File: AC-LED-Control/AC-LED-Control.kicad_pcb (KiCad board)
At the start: 4 copper layers, 120 parts, among them P101 CONN_01X02, P102 CONN_01X02, P103 CONN_01X04, P201 CONN_01X02, P202 CONN_01X02, P203 CONN_01X02, P204 CONN_01X02, P205 CONN_01X02, P206 CONN_01X02, P207 CONN_01X02, P208 CONN_01X02, P301 CONN_01X02, P302 CONN_01X02, P303 CONN_01X02, P304 CONN_01X02, P305 CONN_01X02, P306 CONN_01X02, P307 CONN_01X02, P308 CONN_01X02, SW101 SW_PUSH, U101 FOD814-D, U102 STM32F030F4P6, U103 74HC595, U104 74HC595, U201 LTV-846S, U206 LTV-846S, U301 LTV-846S, U306 LTV-846S

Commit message: Associated LEDs
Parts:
- added D101: LED, LEDs:LED_0805, F.Cu at (6.64, 6.60)
- added D102: LED, LEDs:LED_0805, F.Cu at (12.5, 13.2)
- added D103: LED, LEDs:LED_0805, F.Cu at (-1.52, 6.60)
- added D104: LED, LEDs:LED_0805, F.Cu at (-6.42, 6.60)
- added D105: LED, LEDs:LED_0805, F.Cu at (8.28, 6.60)
- added D106: LED, LEDs:LED_0805, F.Cu at (3.38, 6.60)
- added D107: LED, LEDs:LED_0805, F.Cu at (13.2, 6.60)
- added D108: LED, LEDs:LED_0805, F.Cu at (10.9, 13.2)
- added D109: LED, LEDs:LED_0805, F.Cu at (9.91, 6.60)
- added D110: LED, LEDs:LED_0805, F.Cu at (-4.79, 6.60)
- added D111: LED, LEDs:LED_0805, F.Cu at (1.74, 6.60)
- added D112: LED, LEDs:LED_0805, F.Cu at (0.11, 6.60)
- added D113: LED, LEDs:LED_0805, F.Cu at (-3.16, 6.60)
- added D114: LED, LEDs:LED_0805, F.Cu at (5.01, 6.60)
- added D115: LED, LEDs:LED_0805, F.Cu at (9.25, 13.2)
- added D116: LED, LEDs:LED_0805, F.Cu at (11.5, 6.60)
- added R107: 160, Resistors_SMD:R_0603_HandSoldering, F.Cu at (4.35, 13.2)
- added R108: 160, Resistors_SMD:R_0603_HandSoldering, F.Cu at (7.62, 13.2)
- added R109: 160, Resistors_SMD:R_0603_HandSoldering, F.Cu at (1.09, 13.2)
- added R110: 160, Resistors_SMD:R_0603_HandSoldering, F.Cu at (2.72, 13.2)
- added R111: 160, Resistors_SMD:R_0603_HandSoldering, F.Cu at (-0.54, 13.2)
- added R112: 160, Resistors_SMD:R_0603_HandSoldering, F.Cu at (-3.81, 13.2)
- added R113: 160, Resistors_SMD:R_0603_HandSoldering, F.Cu at (5.99, 13.2)
- added R114: 160, Resistors_SMD:R_0603_HandSoldering, F.Cu at (-2.18, 13.2)
- added U105: VXO7803-1000, power_reg:VXO7803-1000, F.Cu at (22.4, 6.60)
- moved C101 78.3 mm to (112.9, -42.5)
- moved C102 78.3 mm to (112.9, -38.5)
- moved C103 78.3 mm to (111.4, -42.5)
- moved C104 78.3 mm to (114.4, -38.5)
- moved C105 78.3 mm to (114.4, -42.5)
- moved C201 78.3 mm to (48.9, -36.9)
- moved C202 78.3 mm to (0.51, -29.7)
- moved C203 78.3 mm to (29.0, -19.1)
- moved C204 78.3 mm to (44.4, -31.0)
- moved C205 78.3 mm to (2.51, -41.0)
- moved C207 78.3 mm to (-15.2, -41.0)
- moved C208 78.3 mm to (-10.8, -41.0)
- moved C301 78.3 mm to (200.3, -9.75)
- moved C304 78.3 mm to (191.5, -9.75)
- moved C306 78.3 mm to (187.1, -9.75)
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
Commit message: Changed TRIAC from DPAK part to T0-202-3 part.
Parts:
- removed P101, P102, P201, P202, P203, P204, P205, P206, P207, P208, P301, P302, P303, P304, P305, P306, P307, P308: CONN_01X02, Pin_Headers:Pin_Header_Straight_1x02
- removed R217, R218, R219, R220, R317, R318, R319, R320: 660, Resistors_SMD:R_0603_HandSoldering
- removed R221, R222, R223, R224, R225, R226, R227, R228, R229, R230, R231, R232, R321, R322, R323, R324, R325, R326, R327, R328, R329, R330, R331, R332: 56, Resistors_SMD:R_0603_HandSoldering
- removed REF**: Pin_Header_Straight_1x03, Pin_Headers:Pin_Header_Straight_1x03
- added J101: Conn_01x03, Pin_Headers:Pin_Header_Straight_1x03_Pitch2.54mm, F.Cu at (152.8, 151.6)
- added J102: Conn_01x03, Pin_Headers:Pin_Header_Straight_1x03_Pitch2.54mm, F.Cu at (166.6, 148.2)
- added J103: Conn_01x02, Pin_Headers:Pin_Header_Straight_1x02_Pitch2.54mm, F.Cu at (189.2, 137.6)
- added J201: Conn_01x02, Connectors_OnShore:OSTTC022162, F.Cu at (194.2, 119.7)
- added J202: Conn_01x02, Connectors_OnShore:OSTTC022162, F.Cu at (183.5, 119.7)
- added J203: Conn_01x02, Connectors_OnShore:OSTTC022162, F.Cu at (209.0, 93.9)
- added J204: Conn_01x02, Connectors_OnShore:OSTTC022162, F.Cu at (198.3, 106.8)
- added J205: Conn_01x02, Connectors_OnShore:OSTTC022162, F.Cu at (187.5, 106.8)
- added J206: Conn_01x02, Connectors_OnShore:OSTTC022162, F.Cu at (198.3, 93.9)
- added J207: Conn_01x02, Connectors_OnShore:OSTTC022162, F.Cu at (172.7, 115.9)
- added J208: Conn_01x02, Connectors_OnShore:OSTTC022162, F.Cu at (187.5, 93.9)
- added J301: Conn_01x02, Connectors_OnShore:OSTTC022162, F.Cu at (263.4, 119.7)
- added J302: Conn_01x02, Connectors_OnShore:OSTTC022162, F.Cu at (267.4, 93.9)
- added J303: Conn_01x02, Connectors_OnShore:OSTTC022162, F.Cu at (252.6, 115.9)
- added J304: Conn_01x02, Connectors_OnShore:OSTTC022162, F.Cu at (278.2, 93.9)
- added J305: Conn_01x02, Connectors_OnShore:OSTTC022162, F.Cu at (267.4, 106.8)
- added J306: Conn_01x02, Connectors_OnShore:OSTTC022162, F.Cu at (278.2, 106.8)
- added J307: Conn_01x02, Connectors_OnShore:OSTTC022162, F.Cu at (288.9, 93.9)
- added J308: Conn_01x02, Connectors_OnShore:OSTTC022162, F.Cu at (274.1, 119.7)
- added P104: CONN_01X02, Pin_Headers:Pin_Header_Straight_1x02_Pitch2.54mm, F.Cu at (162.6, 160.0)
- added P105: CONN_01X02, Pin_Headers:Pin_Header_Straight_1x02_Pitch2.54mm, F.Cu at (176.4, 148.3)
- added R115: 680, Resistors_SMD:R_0603_HandSoldering, F.Cu at (183.6, 152.5)
- added R116: 680, Resistors_SMD:R_0603_HandSoldering, F.Cu at (196.7, 151.8)
- added U106: IE1203S, SIP-Packages:SIP-4, F.Cu at (143.2, 167.1)
- added U202: TRIAC, Power-Packages:TO-202-3-Vertical, F.Cu at (138.0, 95.2)
- added U203: TRIAC, Power-Packages:TO-202-3-Vertical, F.Cu at (166.0, 95.0)
- added U204: TRIAC, Power-Packages:TO-202-3-Vertical, F.Cu at (125.9, 92.4)
- added U205: TRIAC, Power-Packages:TO-202-3-Vertical, F.Cu at (95.4, 86.4)
- added U207: TRIAC, Power-Packages:TO-202-3-Vertical, F.Cu at (101.7, 86.4)
- added U208: TRIAC, Power-Packages:TO-202-3-Vertical, F.Cu at (108.1, 86.4)
- added U302: TRIAC, Power-Packages:TO-202-3-Vertical, F.Cu at (273.7, 44.2)
- added U303: TRIAC, Power-Packages:TO-202-3-Vertical, F.Cu at (241.9, 45.0)
- added U304: TRIAC, Power-Packages:TO-202-3-Vertical, F.Cu at (235.6, 45.0)
- added U305: TRIAC, Power-Packages:TO-202-3-Vertical, F.Cu at (197.8, 34.8)
- added U307: TRIAC, Power-Packages:TO-202-3-Vertical, F.Cu at (222.9, 45.0)
- added U308: TRIAC, Power-Packages:TO-202-3-Vertical, F.Cu at (267.3, 45.0)
- C201, C202, C203, C204, C205, C206, C207, C208, C301, C302, C303, C304, C305, C306, C307, C308: value 22nF -> 22n
- D101, D102, D103, D104, D105, D106, D107, D108, D109, D110, D111, D112, D113, D114, D115, D116: footprint LEDs:LED_0805 -> LEDs:LED_0603_HandSoldering
- P103: footprint Pin_Headers:Pin_Header_Straight_1x04 -> Pin_Headers:Pin_Header_Straight_1x04_Pitch2.54mm
- R103: value 10K -> 16K
- R201, R202, R301, R302: value 660 -> 56
- R203, R204, R303, R304: value 660 -> 100
- R207, R208, R211, R212, R215, R216, R307, R308, R311, R312, R315, R316: value 56 -> 100
- SW101: footprint Buttons_Switches_SMD:SW_SPST_EVPBF -> Buttons_Switches_THT:SW_PUSH_6mm_h5mm
- U105: value VXO7803-1000 -> LTV-827; footprint power_reg:VXO7803-1000 -> Housings_DIP:DIP-8_W7.62mm
- U201, U206, U301, U306: value LTV-846S -> TRIAC; footprint lite-on:Lite-On_SMD-16 -> Power-Packages:TO-202-3-Vertical
- moved C207 270.1 mm to (210.1, 107.9)
- moved C208 269.1 mm to (210.0, 112.7)
- moved C205 252.8 mm to (210.1, 103.1)
- moved C202 252.4 mm to (201.7, 122.6)
- moved D113 242.6 mm to (188.0, 156.0)
- moved C206 240.3 mm to (205.8, 108.2)
- moved R112 238.4 mm to (178.5, 166.8)
- moved D114 237.7 mm to (200.5, 141.7)
- moved R111 237.5 mm to (192.4, 151.8)
- moved R109 236.9 mm to (196.7, 146.8)
- moved R110 234.0 mm to (182.9, 162.6)
- moved R113 233.9 mm to (187.2, 161.1)
- moved D110 233.5 mm to (174.1, 156.7)
- moved R114 230.7 mm to (178.5, 156.7)
- moved R215 230.1 mm to (174.9, 125.3)
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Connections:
- D102 pad 2: Net-(D102-Pad2) -> /CHAN8
- D104 pad 2: Net-(D104-Pad2) -> /CHAN9
- D106 pad 2: Net-(D106-Pad2) -> /CHAN10
- D108 pad 2: Net-(D108-Pad2) -> /CHAN11
- D109 pad 2: /Output-BankB/OUT-A -> Net-(D109-Pad2)
- D110 pad 2: /Output-BankB/OUT-B -> /CHAN12
- D111 pad 2: /Output-BankB/OUT-C -> Net-(D111-Pad2)
- D112 pad 2: /Output-BankB/OUT-D -> /CHAN13
- D113 pad 2: /Output-BankB/OUT-E -> Net-(D113-Pad2)
- D114 pad 2: /Output-BankB/OUT-F -> /CHAN14
- D115 pad 2: /Output-BankB/OUT-G -> Net-(D115-Pad2)
- D116 pad 2: /Output-BankB/OUT-H -> /CHAN15
- R104 pad 1: +3V3 -> /3v3_ISO
- R105 pad 1: +3V3 -> /3v3_ISO
- R107 pad 2: /Output-BankA/OUT-A -> /CHAN0
- R108 pad 1: Net-(D102-Pad2) -> Net-(D103-Pad2)
- R108 pad 2: /Output-BankA/OUT-B -> /CHAN1
- R109 pad 1: Net-(D103-Pad2) -> Net-(D105-Pad2)
- R109 pad 2: /Output-BankA/OUT-C -> /CHAN2
- R110 pad 1: Net-(D104-Pad2) -> Net-(D107-Pad2)
- R110 pad 2: /Output-BankA/OUT-D -> /CHAN3
- R111 pad 1: Net-(D105-Pad2) -> Net-(D109-Pad2)
- R111 pad 2: /Output-BankA/OUT-E -> /CHAN4
- R112 pad 1: Net-(D106-Pad2) -> Net-(D111-Pad2)
- R112 pad 2: /Output-BankA/OUT-F -> /CHAN5
- R113 pad 1: Net-(D107-Pad2) -> Net-(D113-Pad2)
- R113 pad 2: /Output-BankA/OUT-G -> /CHAN6
- R114 pad 1: Net-(D108-Pad2) -> Net-(D115-Pad2)
- R114 pad 2: /Output-BankA/OUT-H -> /CHAN7
- R201 pad 1: Net-(R201-Pad1) -> /Output-BankA/AC_LOAD-A
- R201 pad 2: /Output-BankA/OUT-A -> Net-(C201-Pad2)
- R202 pad 1: Net-(R202-Pad1) -> /Output-BankA/AC_LOAD-E
- R202 pad 2: /Output-BankA/OUT-B -> Net-(C202-Pad2)
- R203 pad 2: /Output-BankA/OUT-C -> /CHAN0
- R204 pad 2: /Output-BankA/OUT-D -> /CHAN4
- R205 pad 1: Net-(R205-Pad1) -> /Output-BankA/AC_LOAD-B
- R205 pad 2: AC-N -> Net-(C203-Pad2)
- R206 pad 1: Net-(R206-Pad1) -> /Output-BankA/AC_LOAD-F
- R206 pad 2: AC-N -> Net-(C204-Pad2)
- R207 pad 2: AC-N -> /CHAN1
- R208 pad 2: AC-N -> /CHAN5
- R209 pad 1: Net-(C201-Pad2) -> /Output-BankA/AC_LOAD-C
- R209 pad 2: Net-(R209-Pad2) -> Net-(C205-Pad2)
- R210 pad 1: Net-(C202-Pad2) -> /Output-BankA/AC_LOAD-G
- R210 pad 2: Net-(R210-Pad2) -> Net-(C206-Pad2)
- R211 pad 1: Net-(C203-Pad2) -> Net-(R211-Pad1)
- R211 pad 2: Net-(R211-Pad2) -> /CHAN2
- R212 pad 1: Net-(C204-Pad2) -> Net-(R212-Pad1)
- R212 pad 2: Net-(R212-Pad2) -> /CHAN6
- R213 pad 1: /Output-BankA/AC_LOAD-A -> /Output-BankA/AC_LOAD-D
- R213 pad 2: Net-(C201-Pad2) -> Net-(C207-Pad2)
- R214 pad 1: /Output-BankA/AC_LOAD-B -> /Output-BankA/AC_LOAD-H
- R214 pad 2: Net-(C202-Pad2) -> Net-(C208-Pad2)
- R215 pad 1: /Output-BankA/AC_LOAD-C -> Net-(R215-Pad1)
- R215 pad 2: Net-(C203-Pad2) -> /CHAN3
- R216 pad 1: /Output-BankA/AC_LOAD-D -> Net-(R216-Pad1)
- R216 pad 2: Net-(C204-Pad2) -> /CHAN7
- R301 pad 1: Net-(R301-Pad1) -> /Output-BankB/AC_LOAD-A
- R301 pad 2: /Output-BankB/OUT-A -> Net-(C301-Pad2)
- R302 pad 1: Net-(R302-Pad1) -> /Output-BankB/AC_LOAD-E
- R302 pad 2: /Output-BankB/OUT-B -> Net-(C302-Pad2)
- R303 pad 2: /Output-BankB/OUT-C -> /CHAN8
- R304 pad 2: /Output-BankB/OUT-D -> /CHAN12
- R305 pad 1: Net-(R305-Pad1) -> /Output-BankB/AC_LOAD-B
- R305 pad 2: AC-N -> Net-(C303-Pad2)
- R306 pad 1: Net-(R306-Pad1) -> /Output-BankB/AC_LOAD-F
- R306 pad 2: AC-N -> Net-(C304-Pad2)
- R307 pad 2: AC-N -> /CHAN9
- R308 pad 2: AC-N -> /CHAN13
- R309 pad 1: Net-(C301-Pad2) -> /Output-BankB/AC_LOAD-C
- R309 pad 2: Net-(R309-Pad2) -> Net-(C305-Pad2)
- R310 pad 1: Net-(C302-Pad2) -> /Output-BankB/AC_LOAD-G
- R310 pad 2: Net-(R310-Pad2) -> Net-(C306-Pad2)
- R311 pad 1: Net-(C303-Pad2) -> Net-(R311-Pad1)
- R311 pad 2: Net-(R311-Pad2) -> /CHAN10
- R312 pad 1: Net-(C304-Pad2) -> Net-(R312-Pad1)
- R312 pad 2: Net-(R312-Pad2) -> /CHAN14
- R313 pad 1: /Output-BankB/AC_LOAD-A -> /Output-BankB/AC_LOAD-D
- R313 pad 2: Net-(C301-Pad2) -> Net-(C307-Pad2)
- R314 pad 1: /Output-BankB/AC_LOAD-B -> /Output-BankB/AC_LOAD-H
- R314 pad 2: Net-(C302-Pad2) -> Net-(C308-Pad2)
- R315 pad 1: /Output-BankB/AC_LOAD-C -> Net-(R315-Pad1)
- R315 pad 2: Net-(C303-Pad2) -> /CHAN11
- R316 pad 1: /Output-BankB/AC_LOAD-D -> Net-(R316-Pad1)
- R316 pad 2: Net-(C304-Pad2) -> /CHAN15
- U102 pad 17: /I2C_SCL -> /STM_SCL
- U102 pad 18: /I2C_SDA -> /STM_SDA
- U103 pad 1: /Output-BankA/OUT-B -> /CHAN1
- U103 pad 15: /Output-BankA/OUT-A -> /CHAN0
- U103 pad 2: /Output-BankA/OUT-C -> /CHAN2
- U103 pad 3: /Output-BankA/OUT-D -> /CHAN3
- U103 pad 4: /Output-BankA/OUT-E -> /CHAN4
- U103 pad 5: /Output-BankA/OUT-F -> /CHAN5
- U103 pad 6: /Output-BankA/OUT-G -> /CHAN6
- U103 pad 7: /Output-BankA/OUT-H -> /CHAN7
- U104 pad 1: /Output-BankB/OUT-B -> /CHAN9
- U104 pad 15: /Output-BankB/OUT-A -> /CHAN8
- U104 pad 2: /Output-BankB/OUT-C -> /CHAN10
- U104 pad 3: /Output-BankB/OUT-D -> /CHAN11
- U104 pad 4: /Output-BankB/OUT-E -> /CHAN12
- U104 pad 5: /Output-BankB/OUT-F -> /CHAN13
- U104 pad 6: /Output-BankB/OUT-G -> /CHAN14
- U104 pad 7: /Output-BankB/OUT-H -> /CHAN15
- U105 pad 1: /+12V_IN -> /STM_SCL
- U105 pad 3: +3V3 -> /STM_SDA
- U201 pad 1: Net-(R201-Pad1) -> AC-N
- U201 pad 2: GND -> /Output-BankA/AC_LOAD-A
- U201 pad 3: Net-(R202-Pad1) -> Net-(R203-Pad1)
- U206 pad 1: Net-(R217-Pad1) -> AC-N
- U206 pad 2: GND -> /Output-BankA/AC_LOAD-G
- U206 pad 3: Net-(R218-Pad1) -> Net-(R212-Pad1)
- U301 pad 1: Net-(R301-Pad1) -> AC-N
- U301 pad 2: GND -> /Output-BankB/AC_LOAD-A
- U301 pad 3: Net-(R302-Pad1) -> Net-(R303-Pad1)
- U306 pad 1: Net-(R317-Pad1) -> AC-N
- U306 pad 2: GND -> /Output-BankB/AC_LOAD-G
- U306 pad 3: Net-(R318-Pad1) -> Net-(R312-Pad1)
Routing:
- net +3V3: track 26.1 -> 0.00 mm
- net /STM_~RST: track 17.3 -> 0.00 mm
- net /STM_SWDIO: track 10.7 -> 0.00 mm
- net /I2C_SDA: track 9.93 -> 0.00 mm
- net /I2C_SCL: track 9.82 -> 0.00 mm
- net /STM_SWCLK: track 8.39 -> 0.00 mm
- net GND: track 5.75 -> 0.00 mm
- net /ZERO_CROSS: track 2.58 -> 0.00 mm
- net Net-(R102-Pad1): track 2.27 -> 0.00 mm
- net Net-(R101-Pad1): track 2.27 -> 0.00 mm
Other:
- board text removed: "OUTA"
- board text removed: "OUTD"
- board text removed: "OUTE"
- board text removed: "OUTH"

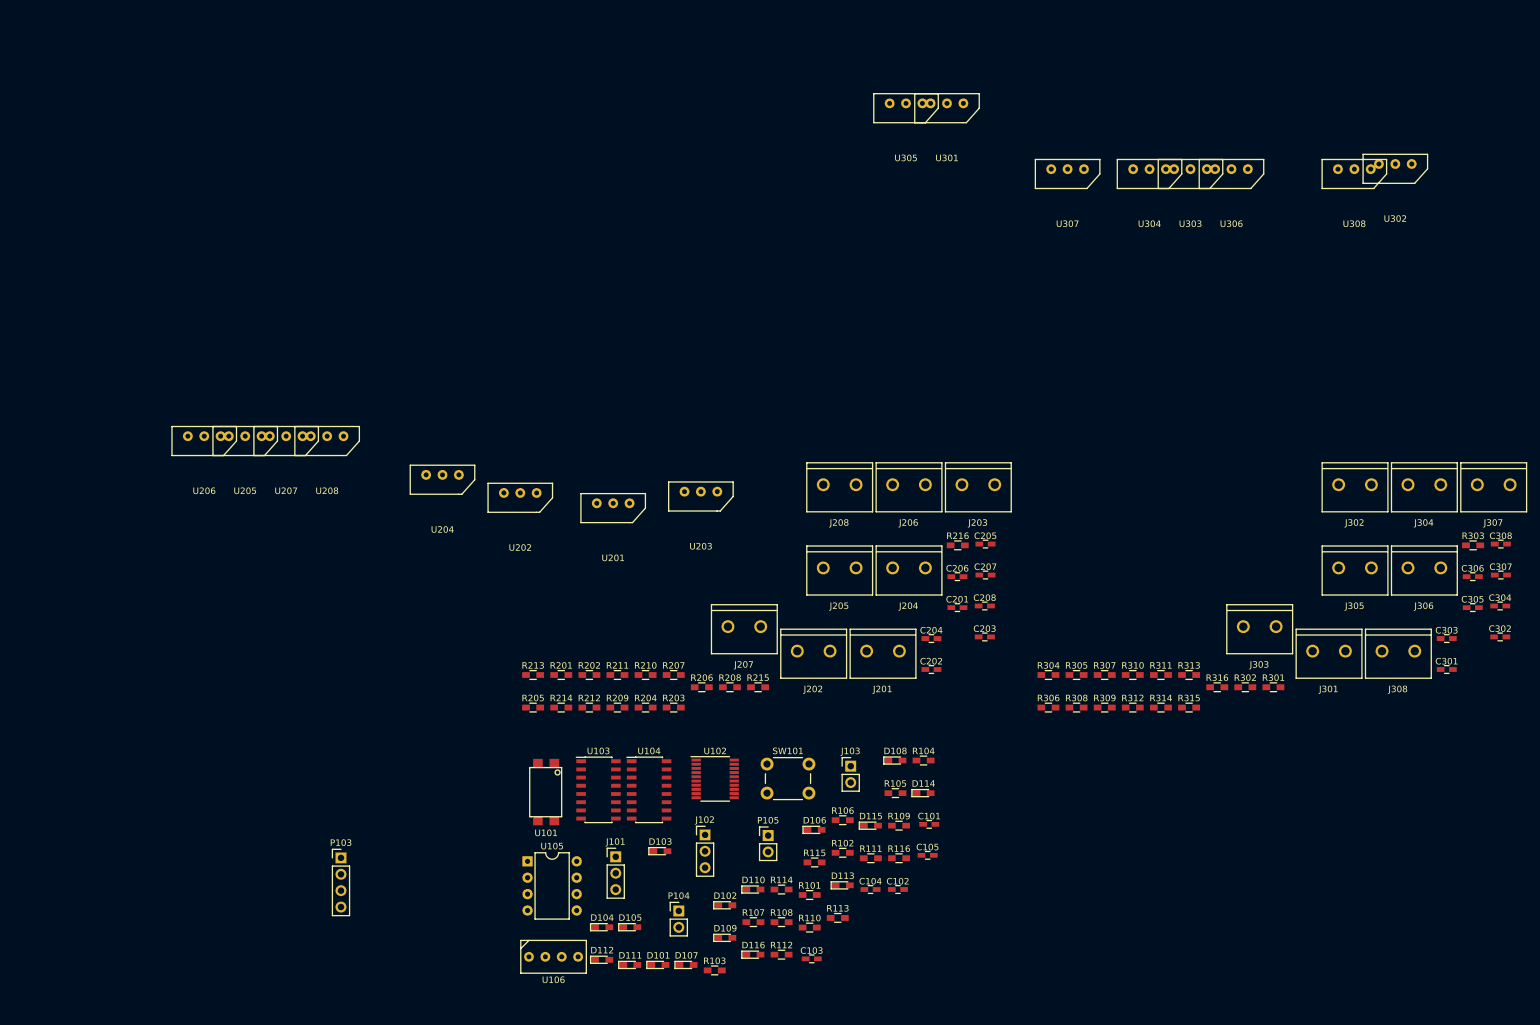
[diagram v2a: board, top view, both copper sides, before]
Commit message: Lots of layout + added a diode.
I realised that the power regulator might need protection from the 3v3
line on the programming header.
Added a diode just in case.
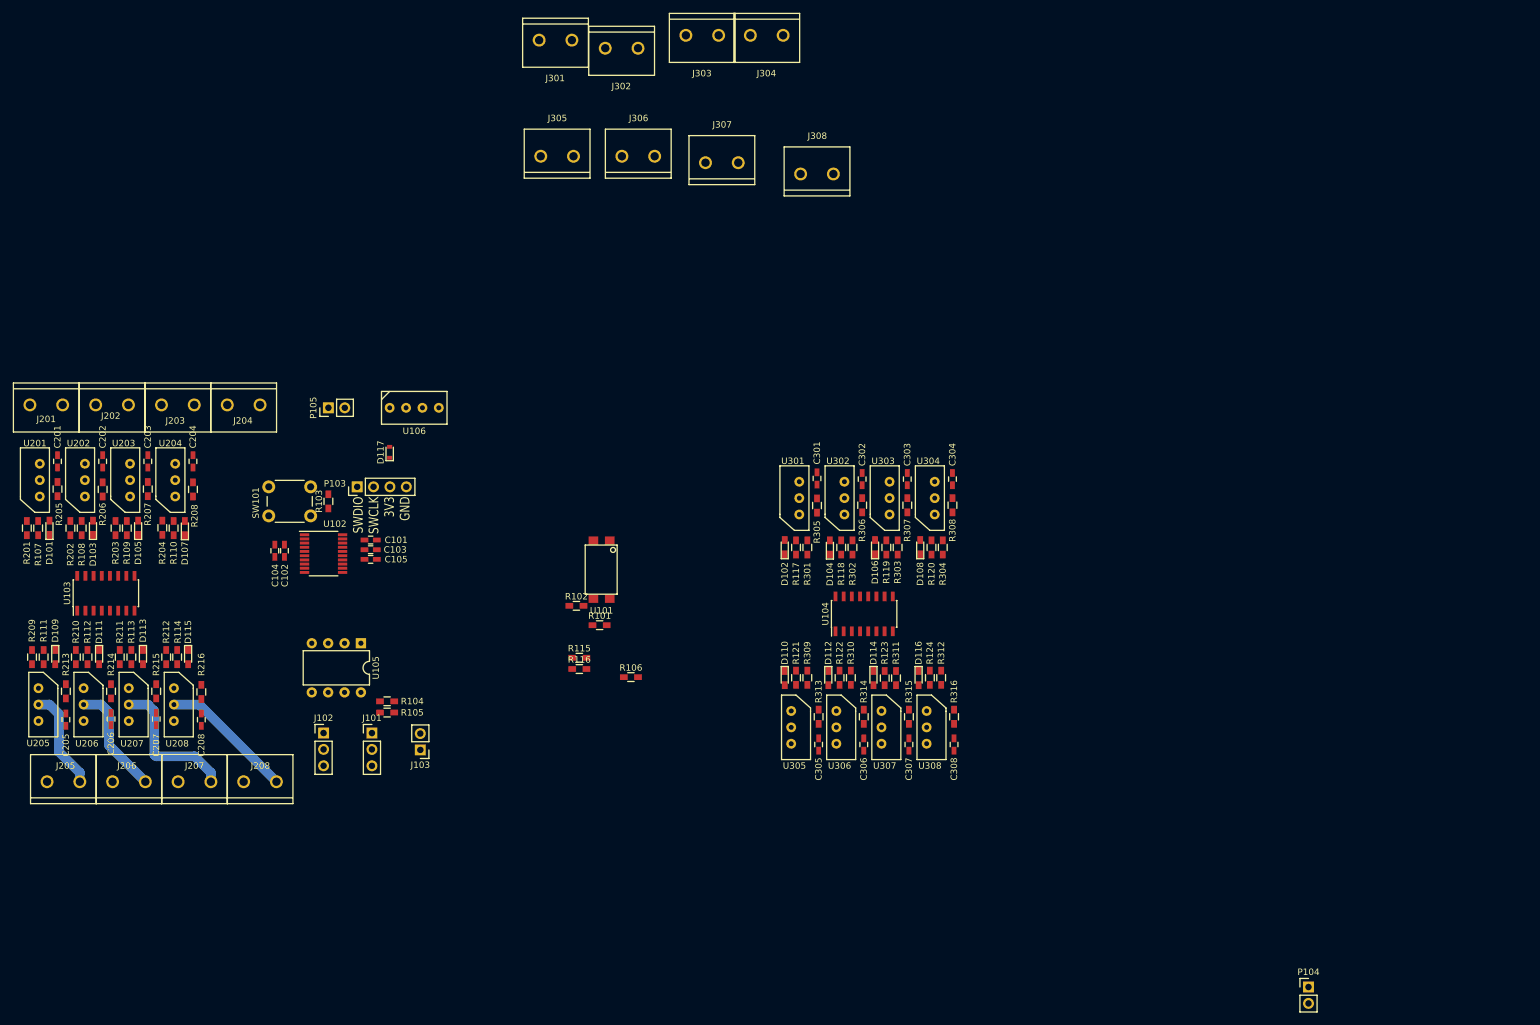
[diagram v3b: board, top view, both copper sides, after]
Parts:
- added D117: D, Diodes_SMD:D_0603, F.Cu at (117.8, 88.9)
- added R117: 160, Resistors_SMD:R_0603_HandSoldering, F.Cu at (180.8, 103.7)
- added R118: 160, Resistors_SMD:R_0603_HandSoldering, F.Cu at (187.8, 103.7)
- added R119: 160, Resistors_SMD:R_0603_HandSoldering, F.Cu at (194.8, 103.7)
- added R120: 160, Resistors_SMD:R_0603_HandSoldering, F.Cu at (201.8, 103.7)
- added R121: 160, Resistors_SMD:R_0603_HandSoldering, F.Cu at (180.8, 123.8)
- added R122: 160, Resistors_SMD:R_0603_HandSoldering, F.Cu at (187.5, 123.8)
- added R123: 160, Resistors_SMD:R_0603_HandSoldering, F.Cu at (194.5, 123.9)
- added R124: 160, Resistors_SMD:R_0603_HandSoldering, F.Cu at (201.5, 123.8)
- R201, R202, R209, R210, R301, R302, R309, R310: value 56 -> 100
- R207, R208, R215, R216, R307, R308, R315, R316: value 100 -> 56
- moved J301 152.8 mm to (143.5, 25.0)
- moved C205 145.2 mm to (67.5, 130.3), turned to 90 degrees
- moved C201 141.3 mm to (66.2, 90.3), turned to 270 degrees
- moved J305 139.2 mm to (143.7, 43.0), turned to 180 degrees
- moved J306 137.6 mm to (156.3, 43.0), turned to 180 degrees
- moved J201 135.2 mm to (64.5, 81.5)
- moved C206 133.1 mm to (74.5, 130.2), turned to 90 degrees
- moved C203 132.6 mm to (80.2, 90.3), turned to 270 degrees
- moved C202 132.5 mm to (73.2, 90.3), turned to 270 degrees
- moved J302 132.3 mm to (153.7, 26.2)
- moved R111 132.0 mm to (64.1, 120.7), turned to 90 degrees
- moved C207 130.5 mm to (81.5, 130.2), turned to 90 degrees
- moved J307 129.7 mm to (169.2, 44.0), turned to 180 degrees
- moved J206 129.4 mm to (77.3, 140.0), turned to 180 degrees
- moved R109 128.3 mm to (77.0, 100.7), turned to 270 degrees
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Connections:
- D102 pad 2: /CHAN8 -> Net-(D102-Pad2)
- D104 pad 2: /CHAN9 -> Net-(D104-Pad2)
- D106 pad 2: /CHAN10 -> Net-(D106-Pad2)
- D108 pad 2: /CHAN11 -> Net-(D108-Pad2)
- D110 pad 2: /CHAN12 -> Net-(D110-Pad2)
- D112 pad 2: /CHAN13 -> Net-(D112-Pad2)
- D114 pad 2: /CHAN14 -> Net-(D114-Pad2)
- D116 pad 2: /CHAN15 -> Net-(D116-Pad2)
- J202 pad 1: /Output-BankA/AC_LOAD-E -> /Output-BankA/AC_LOAD-B
- J203 pad 1: /Output-BankA/AC_LOAD-B -> /Output-BankA/AC_LOAD-C
- J204 pad 1: /Output-BankA/AC_LOAD-F -> /Output-BankA/AC_LOAD-D
- J205 pad 1: /Output-BankA/AC_LOAD-C -> /Output-BankA/AC_LOAD-E
- J206 pad 1: /Output-BankA/AC_LOAD-G -> /Output-BankA/AC_LOAD-F
- J207 pad 1: /Output-BankA/AC_LOAD-D -> /Output-BankA/AC_LOAD-G
- J302 pad 1: /Output-BankB/AC_LOAD-E -> /Output-BankB/AC_LOAD-B
- J303 pad 1: /Output-BankB/AC_LOAD-B -> /Output-BankB/AC_LOAD-C
- J304 pad 1: /Output-BankB/AC_LOAD-F -> /Output-BankB/AC_LOAD-D
- J305 pad 1: /Output-BankB/AC_LOAD-C -> /Output-BankB/AC_LOAD-E
- J306 pad 1: /Output-BankB/AC_LOAD-G -> /Output-BankB/AC_LOAD-F
- J307 pad 1: /Output-BankB/AC_LOAD-D -> /Output-BankB/AC_LOAD-G
- P103 pad 3: +3V3 -> /STM_VCC
- R201 pad 1: /Output-BankA/AC_LOAD-A -> Net-(R201-Pad1)
- R201 pad 2: Net-(C201-Pad2) -> /CHAN0
- R202 pad 1: /Output-BankA/AC_LOAD-E -> Net-(R202-Pad1)
- R202 pad 2: Net-(C202-Pad2) -> /CHAN1
- R203 pad 2: /CHAN0 -> /CHAN2
- R204 pad 2: /CHAN4 -> /CHAN3
- R205 pad 1: /Output-BankA/AC_LOAD-B -> /Output-BankA/AC_LOAD-A
- R205 pad 2: Net-(C203-Pad2) -> Net-(C201-Pad2)
- R206 pad 1: /Output-BankA/AC_LOAD-F -> /Output-BankA/AC_LOAD-B
- R206 pad 2: Net-(C204-Pad2) -> Net-(C202-Pad2)
- R207 pad 1: Net-(R207-Pad1) -> /Output-BankA/AC_LOAD-C
- R207 pad 2: /CHAN1 -> Net-(C203-Pad2)
- R208 pad 1: Net-(R208-Pad1) -> /Output-BankA/AC_LOAD-D
- R208 pad 2: /CHAN5 -> Net-(C204-Pad2)
- R209 pad 1: /Output-BankA/AC_LOAD-C -> Net-(R209-Pad1)
- R209 pad 2: Net-(C205-Pad2) -> /CHAN4
- R210 pad 1: /Output-BankA/AC_LOAD-G -> Net-(R210-Pad1)
- R210 pad 2: Net-(C206-Pad2) -> /CHAN5
- R211 pad 2: /CHAN2 -> /CHAN6
- R212 pad 2: /CHAN6 -> /CHAN7
- R213 pad 1: /Output-BankA/AC_LOAD-D -> /Output-BankA/AC_LOAD-E
- R213 pad 2: Net-(C207-Pad2) -> Net-(C205-Pad2)
- R214 pad 1: /Output-BankA/AC_LOAD-H -> /Output-BankA/AC_LOAD-F
- R214 pad 2: Net-(C208-Pad2) -> Net-(C206-Pad2)
- R215 pad 1: Net-(R215-Pad1) -> /Output-BankA/AC_LOAD-G
- R215 pad 2: /CHAN3 -> Net-(C207-Pad2)
- R216 pad 1: Net-(R216-Pad1) -> /Output-BankA/AC_LOAD-H
- R216 pad 2: /CHAN7 -> Net-(C208-Pad2)
- R301 pad 1: /Output-BankB/AC_LOAD-A -> Net-(R301-Pad1)
- R301 pad 2: Net-(C301-Pad2) -> /CHAN8
- R302 pad 1: /Output-BankB/AC_LOAD-E -> Net-(R302-Pad1)
- R302 pad 2: Net-(C302-Pad2) -> /CHAN9
- R303 pad 2: /CHAN8 -> /CHAN10
- R304 pad 2: /CHAN12 -> /CHAN11
- R305 pad 1: /Output-BankB/AC_LOAD-B -> /Output-BankB/AC_LOAD-A
- R305 pad 2: Net-(C303-Pad2) -> Net-(C301-Pad2)
- R306 pad 1: /Output-BankB/AC_LOAD-F -> /Output-BankB/AC_LOAD-B
- R306 pad 2: Net-(C304-Pad2) -> Net-(C302-Pad2)
- R307 pad 1: Net-(R307-Pad1) -> /Output-BankB/AC_LOAD-C
- R307 pad 2: /CHAN9 -> Net-(C303-Pad2)
- R308 pad 1: Net-(R308-Pad1) -> /Output-BankB/AC_LOAD-D
- R308 pad 2: /CHAN13 -> Net-(C304-Pad2)
- R309 pad 1: /Output-BankB/AC_LOAD-C -> Net-(R309-Pad1)
- R309 pad 2: Net-(C305-Pad2) -> /CHAN12
- R310 pad 1: /Output-BankB/AC_LOAD-G -> Net-(R310-Pad1)
- R310 pad 2: Net-(C306-Pad2) -> /CHAN13
- R311 pad 2: /CHAN10 -> /CHAN14
- R312 pad 2: /CHAN14 -> /CHAN15
- R313 pad 1: /Output-BankB/AC_LOAD-D -> /Output-BankB/AC_LOAD-E
- R313 pad 2: Net-(C307-Pad2) -> Net-(C305-Pad2)
- R314 pad 1: /Output-BankB/AC_LOAD-H -> /Output-BankB/AC_LOAD-F
- R314 pad 2: Net-(C308-Pad2) -> Net-(C306-Pad2)
- R315 pad 1: Net-(R315-Pad1) -> /Output-BankB/AC_LOAD-G
- R315 pad 2: /CHAN11 -> Net-(C307-Pad2)
- R316 pad 1: Net-(R316-Pad1) -> /Output-BankB/AC_LOAD-H
- R316 pad 2: /CHAN15 -> Net-(C308-Pad2)
- U201 pad 3: Net-(R203-Pad1) -> Net-(R201-Pad1)
- U202 pad 2: /Output-BankA/AC_LOAD-E -> /Output-BankA/AC_LOAD-B
- U202 pad 3: Net-(R204-Pad1) -> Net-(R202-Pad1)
- U203 pad 2: /Output-BankA/AC_LOAD-B -> /Output-BankA/AC_LOAD-C
- U203 pad 3: Net-(R207-Pad1) -> Net-(R203-Pad1)
- U204 pad 2: /Output-BankA/AC_LOAD-F -> /Output-BankA/AC_LOAD-D
- U204 pad 3: Net-(R208-Pad1) -> Net-(R204-Pad1)
- U205 pad 2: /Output-BankA/AC_LOAD-C -> /Output-BankA/AC_LOAD-E
- U205 pad 3: Net-(R211-Pad1) -> Net-(R209-Pad1)
- U206 pad 2: /Output-BankA/AC_LOAD-G -> /Output-BankA/AC_LOAD-F
- U206 pad 3: Net-(R212-Pad1) -> Net-(R210-Pad1)
- U207 pad 2: /Output-BankA/AC_LOAD-D -> /Output-BankA/AC_LOAD-G
- U207 pad 3: Net-(R215-Pad1) -> Net-(R211-Pad1)
- U208 pad 3: Net-(R216-Pad1) -> Net-(R212-Pad1)
- U301 pad 3: Net-(R303-Pad1) -> Net-(R301-Pad1)
- U302 pad 2: /Output-BankB/AC_LOAD-E -> /Output-BankB/AC_LOAD-B
- U302 pad 3: Net-(R304-Pad1) -> Net-(R302-Pad1)
- U303 pad 2: /Output-BankB/AC_LOAD-B -> /Output-BankB/AC_LOAD-C
- U303 pad 3: Net-(R307-Pad1) -> Net-(R303-Pad1)
- U304 pad 2: /Output-BankB/AC_LOAD-F -> /Output-BankB/AC_LOAD-D
- U304 pad 3: Net-(R308-Pad1) -> Net-(R304-Pad1)
- U305 pad 2: /Output-BankB/AC_LOAD-C -> /Output-BankB/AC_LOAD-E
- U305 pad 3: Net-(R311-Pad1) -> Net-(R309-Pad1)
- U306 pad 2: /Output-BankB/AC_LOAD-G -> /Output-BankB/AC_LOAD-F
- U306 pad 3: Net-(R312-Pad1) -> Net-(R310-Pad1)
- U307 pad 2: /Output-BankB/AC_LOAD-D -> /Output-BankB/AC_LOAD-G
- U307 pad 3: Net-(R315-Pad1) -> Net-(R311-Pad1)
- U308 pad 3: Net-(R316-Pad1) -> Net-(R312-Pad1)
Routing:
- net /Output-BankA/AC_LOAD-G: track 0.00 -> 22.5 mm
- net /Output-BankA/AC_LOAD-H: track 0.00 -> 20.8 mm
- net /Output-BankA/AC_LOAD-F: track 0.00 -> 17.5 mm
- net /Output-BankA/AC_LOAD-E: track 0.00 -> 15.6 mm
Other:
- board text added: "SWDIO SWCLK 3V3 GND"

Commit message: Finished most placement and ac control lines.
Finished up general placement of components.
Also did most of the control lines for the AC side of things.
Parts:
- moved J306 102.0 mm to (124.7, 139.9)
- moved J308 101.9 mm to (145.0, 139.9)
- moved J307 101.9 mm to (134.8, 139.9)
- moved J305 101.2 mm to (114.5, 139.9)
- moved P104 100.3 mm to (174.0, 120.5)
- moved J303 65.5 mm to (134.7, 81.7)
- moved J304 65.5 mm to (144.9, 81.7)
- moved U104 63.9 mm to (127.5, 110.5)
- moved J301 63.7 mm to (114.4, 81.7)
- moved J302 62.7 mm to (124.6, 81.7)
- moved C301 56.3 mm to (127.8, 89.7)
- moved C302 56.3 mm to (134.8, 89.8)
- moved C303 56.3 mm to (141.8, 89.8)
- moved C304 56.3 mm to (148.8, 89.8)
- moved C305 56.3 mm to (128.0, 130.9)
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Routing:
- net AC-N: track 0.00 -> 63.4 mm
- net /Output-BankB/AC_LOAD-A: track 0.00 -> 23.1 mm
- net /Output-BankB/AC_LOAD-E: track 0.00 -> 21.9 mm
- net /Output-BankB/AC_LOAD-B: track 0.00 -> 20.8 mm
- net /Output-BankB/AC_LOAD-H: track 0.00 -> 20.6 mm
- net /Output-BankA/AC_LOAD-D: track 0.00 -> 20.5 mm
- net /Output-BankB/AC_LOAD-G: track 0.00 -> 20.1 mm
- net /Output-BankB/AC_LOAD-F: track 0.00 -> 19.5 mm
- net /Output-BankB/AC_LOAD-C: track 0.00 -> 19.3 mm
- net /Output-BankA/AC_LOAD-B: track 0.00 -> 19.0 mm
- net /Output-BankA/AC_LOAD-C: track 0.00 -> 19.0 mm
- net /Output-BankA/AC_LOAD-A: track 0.00 -> 17.8 mm
- net /Output-BankB/AC_LOAD-D: track 0.00 -> 17.3 mm
- net /Output-BankA/AC_LOAD-G: track 22.5 -> 28.0 mm
- net /Output-BankA/AC_LOAD-F: track 17.5 -> 23.1 mm
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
